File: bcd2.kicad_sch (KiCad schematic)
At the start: 2 parts

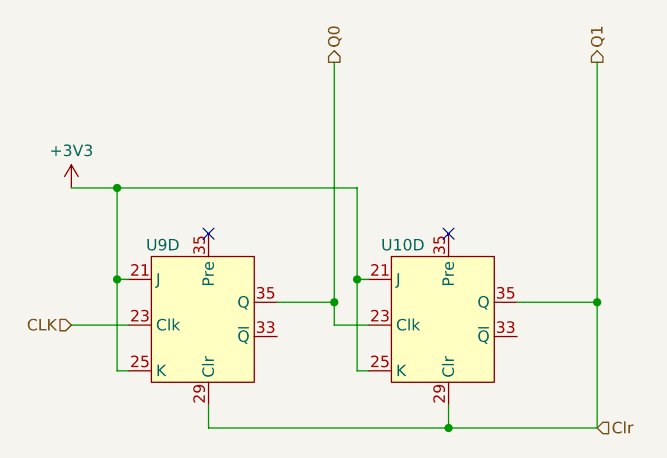
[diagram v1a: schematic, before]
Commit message: added footprints for modules
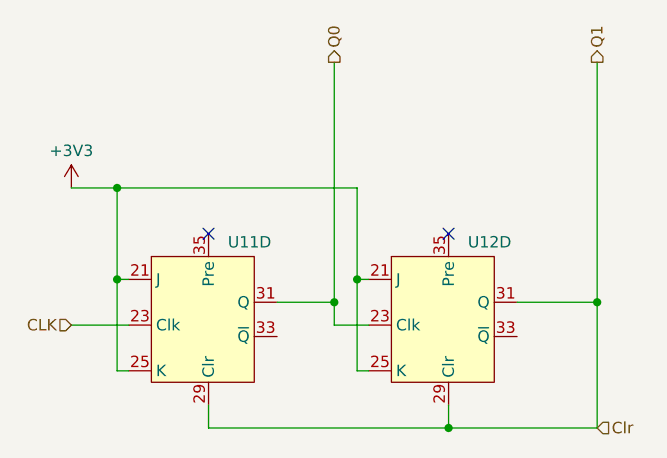
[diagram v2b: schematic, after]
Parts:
- U11: renamed from U9; footprint (none) -> custom:module_flipflop_mpcie
- U12: renamed from U10; footprint (none) -> custom:module_flipflop_mpcie
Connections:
- net Clr: now also U12.31 (Q); no longer U12.35 (Q)
- net Q0: now also U11.31 (Q); no longer U11.35 (Q)
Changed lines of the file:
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@@
 		(dnp no)
 		(fields_autoplaced yes)
-		(property "Reference" "#PWR0181"
+		(property "Reference" "#PWR019"
 			(at 55.88 102.87 0)
 			(effects
@@
 			(project "transistor-clock"
 				(path "/ce10d5bc-995e-4952-aa76-0a08f713a0f2/2c36a9e9-de42-4705-9ad4-94f4cc168e2f/e5d5ceff-c3df-4aeb-b3ac-c735ee65b6d1"
-					(reference "#PWR0181")
+					(reference "#PWR019")
 					(unit 1)
 				)
@@
 	)
 	(symbol
-		(lib_name "jk-flipflops_1")
 		(lib_id "custom:jk-flipflops")
 		(at 66.04 105.41 0)
@@
 		(dnp no)
 		(fields_autoplaced yes)
-		(property "Reference" "U9"
-			(at 66.04 105.41 0)
-			(effects
-				(font
-					(size 1.27 1.27)
-				)
+		(property "Reference" "U11"
+			(at 73.2633 105.0869 0)
+			(effects
+				(font
+					(size 1.27 1.27)
+				)
+				(justify left)
 			)
 		)
@@
 			)
 		)
-		(property "Footprint" ""
+		(property "Footprint" "custom:module_flipflop_mpcie"
 			(at 66.04 105.41 0)
 			(effects
@@
 		(pin "8"
 		)
-		(pin "35"
+		(pin "31"
 		)
 		(instances
 			(project "transistor-clock"
 				(path "/ce10d5bc-995e-4952-aa76-0a08f713a0f2/2c36a9e9-de42-4705-9ad4-94f4cc168e2f/e5d5ceff-c3df-4aeb-b3ac-c735ee65b6d1"
-					(reference "U9")
+					(reference "U11")
 					(unit 4)
 				)
@@
 		(dnp no)
 		(fields_autoplaced yes)
-		(property "Reference" "U10"
-			(at 92.71 105.41 0)
-			(effects
-				(font
-					(size 1.27 1.27)
-				)
+		(property "Reference" "U12"
+			(at 99.9333 105.0869 0)
+			(effects
+				(font
+					(size 1.27 1.27)
+				)
+				(justify left)
 			)
 		)
@@
 			)
 		)
-		(property "Footprint" ""
+		(property "Footprint" "custom:module_flipflop_mpcie"
 			(at 92.71 105.41 0)
 			(effects
@@
 		(pin "34"
 		)
-		(pin "35"
+		(pin "31"
 		)
 		(pin "12"
@@
 			(project "transistor-clock"
 				(path "/ce10d5bc-995e-4952-aa76-0a08f713a0f2/2c36a9e9-de42-4705-9ad4-94f4cc168e2f/e5d5ceff-c3df-4aeb-b3ac-c735ee65b6d1"
-					(reference "U10")
+					(reference "U12")
 					(unit 4)
 				)

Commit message: added module for PSU
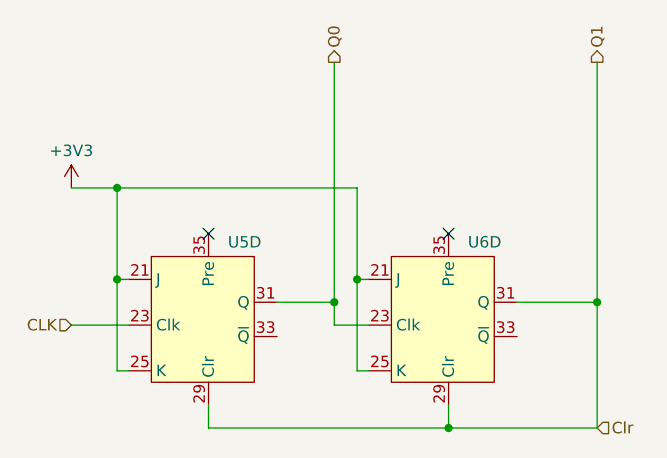
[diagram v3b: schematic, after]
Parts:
- U5: renamed from U11; value ~ -> flipflop; LCSC Part # (none) -> C185937
- U6: renamed from U12; value ~ -> flipflop; LCSC Part # (none) -> C185937
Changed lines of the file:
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@@
 		(dnp no)
 		(fields_autoplaced yes)
-		(property "Reference" "U11"
+		(property "Reference" "U5"
 			(at 73.2633 105.0869 0)
 			(effects
@@
 			)
 		)
-		(property "Value" "~"
+		(property "Value" "flipflop"
 			(at 66.04 105.41 0)
 			(effects
@@
 			)
 		)
-		(property "LCSC Part #" ""
+		(property "LCSC Part #" "C185937"
 			(at 66.04 105.41 0)
 			(effects
@@
 			(project "transistor-clock"
 				(path "/ce10d5bc-995e-4952-aa76-0a08f713a0f2/2c36a9e9-de42-4705-9ad4-94f4cc168e2f/e5d5ceff-c3df-4aeb-b3ac-c735ee65b6d1"
-					(reference "U11")
+					(reference "U5")
 					(unit 4)
 				)
@@
 		(dnp no)
 		(fields_autoplaced yes)
-		(property "Reference" "U12"
+		(property "Reference" "U6"
 			(at 99.9333 105.0869 0)
 			(effects
@@
 			)
 		)
-		(property "Value" "~"
+		(property "Value" "flipflop"
 			(at 92.71 105.41 0)
 			(effects
@@
 			)
 		)
-		(property "LCSC Part #" ""
+		(property "LCSC Part #" "C185937"
 			(at 92.71 105.41 0)
 			(effects
@@
 			(project "transistor-clock"
 				(path "/ce10d5bc-995e-4952-aa76-0a08f713a0f2/2c36a9e9-de42-4705-9ad4-94f4cc168e2f/e5d5ceff-c3df-4aeb-b3ac-c735ee65b6d1"
-					(reference "U12")
+					(reference "U6")
 					(unit 4)
 				)
